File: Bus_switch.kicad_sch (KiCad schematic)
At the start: 8 parts, among them J3 Conn_01x04_Pin, U1 SN74CB3Q3384APW

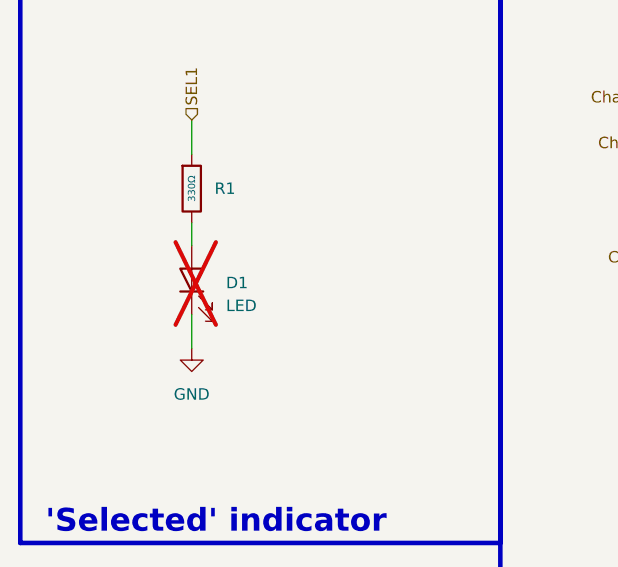
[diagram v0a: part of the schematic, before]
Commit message: added leds and bom. Revison 1.2
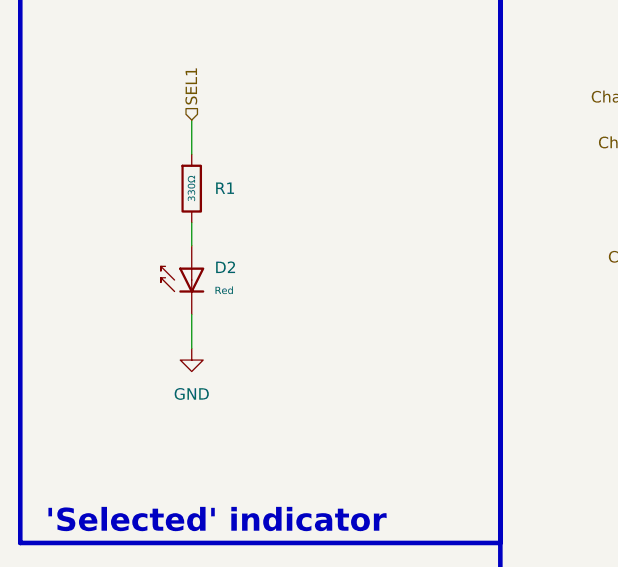
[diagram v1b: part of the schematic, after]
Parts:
- removed D1: LED, LED_SMD:LED_0603_1608Metric, symbol Device:LED
- added D2: Red, PCM_JLCPCB:D_0603, symbol PCM_JLCPCB-Diodes:LED,0603,Red
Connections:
- net GND: now also D2.1
- net at R1.2: now also D2.2

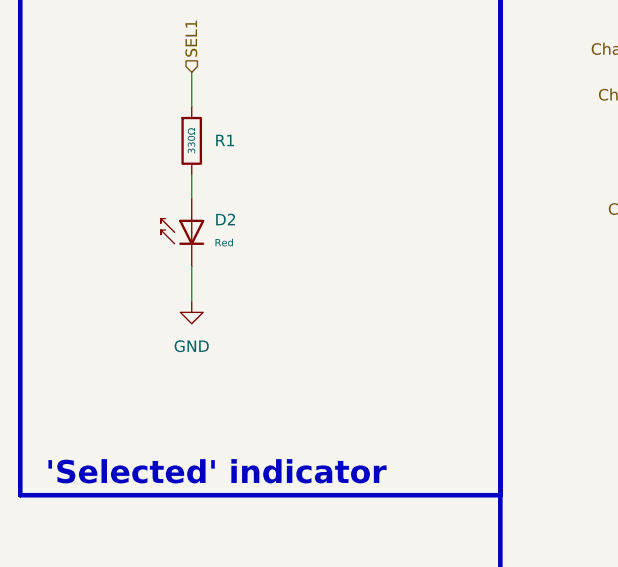
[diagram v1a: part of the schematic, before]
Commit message: fixed selected led polarity
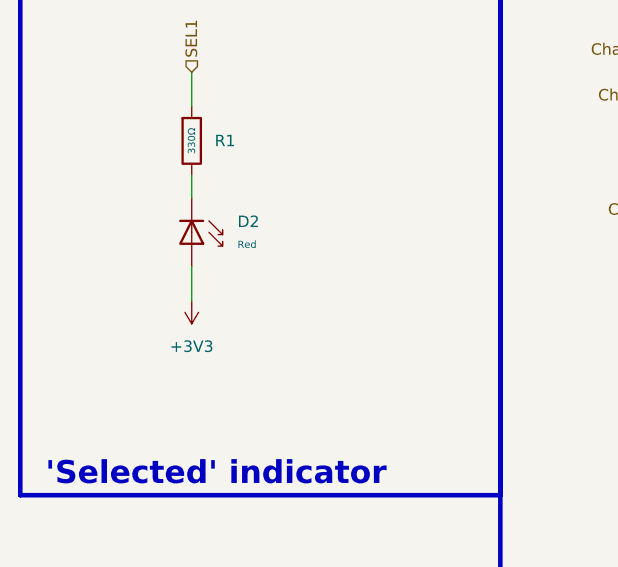
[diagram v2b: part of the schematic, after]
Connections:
- net +3V3: now also D2.2
- net GND: no longer D2.1
- net at R1.2: now also D2.1; no longer D2.2
